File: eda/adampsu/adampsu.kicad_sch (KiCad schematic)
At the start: 61 parts, among them J1 Barrel_Jack_Switch, J2 Conn_2Rows-09Pins, J3 DB9_Female, Q1 Si4447ADY, Q2 Q_NPN_BEC, SW1 30V 300mA Latching Switch, U1 TPS561201, U2 TPS54531DDAR, U3 Cuts

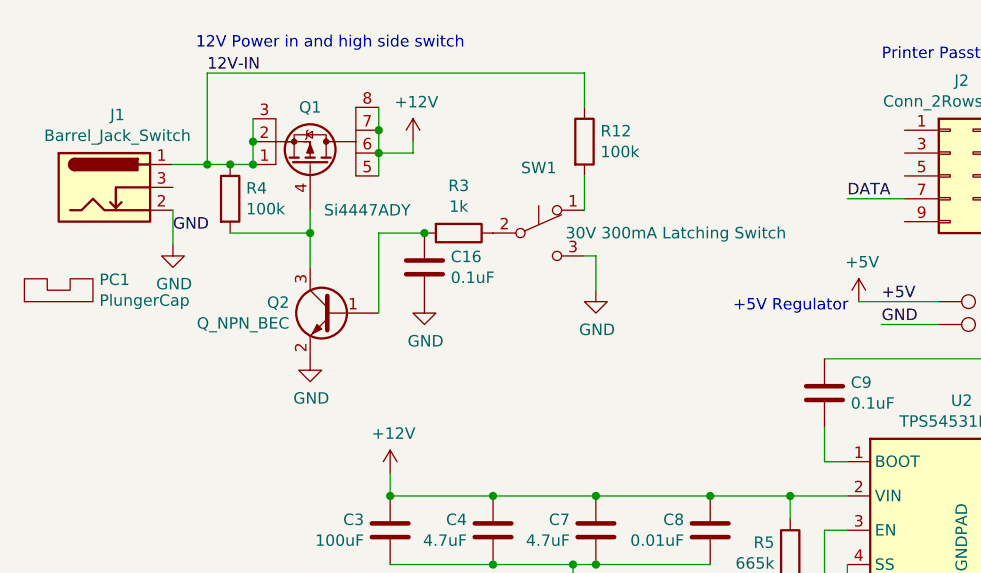
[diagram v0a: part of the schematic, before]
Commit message: Rerouted high side switch to be simpler and exported gerbers.
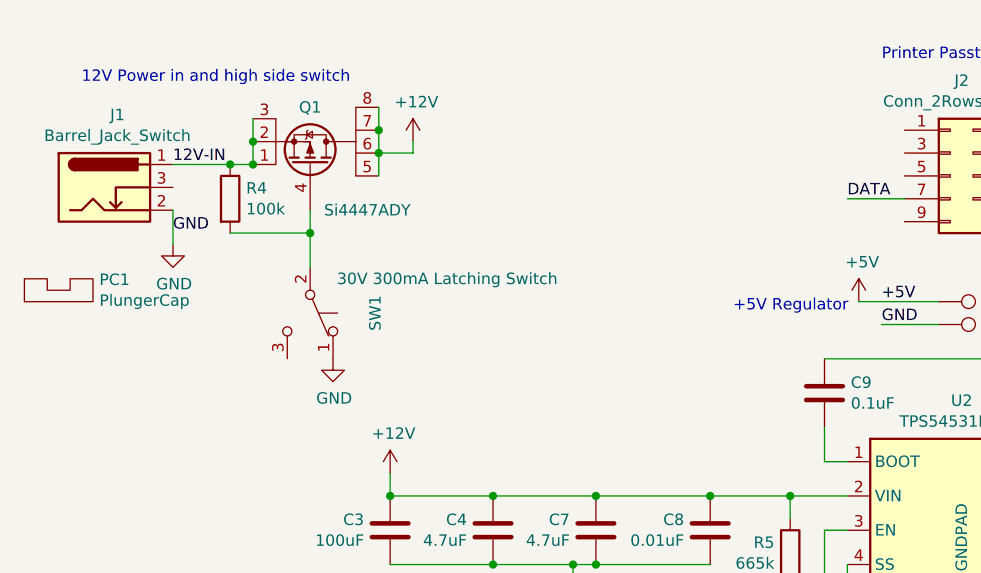
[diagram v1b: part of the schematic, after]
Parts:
- removed C16: 0.1uF, Capacitor_SMD:C_0603_1608Metric_Pad1.05x0.95mm_HandSolder, symbol Device:C
- removed Q2: Q_NPN_BEC, Package_TO_SOT_SMD:SOT-23, symbol Device:Q_NPN_BEC
- removed R12: 100k, Resistor_SMD:R_0603_1608Metric_Pad1.05x0.95mm_HandSolder, symbol Device:R
- removed R3: 1k, Resistor_SMD:R_0603_1608Metric_Pad1.05x0.95mm_HandSolder, symbol Device:R
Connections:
- net GND: now also SW1.1 (A); no longer SW1.3 (C)
- net at SW1.2 (B): now also Q1.4 (G), R4.2
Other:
- moved on the sheet: SW1
